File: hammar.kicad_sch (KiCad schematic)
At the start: 116 parts, among them J1 8x screw terminal, 5,08mm spa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, J10 1x2, J11 1x4, J12 1x3, J13 1x8, J14 1x3, J15 1x3, J16 1x3, J2 Micro_SD_Holder, J3 USB_C_Receptacle_USB2.0, J4 1x4, J5 1x4, J6 1x4, J7 1x4, J8 1x4, J9 1x2, Q1 S9014 or equivalent, Q2 S9014 or equivalent, Q3 TI CSD17310Q5A or equivalent, Q4 PMV40UN2R or equivalent, Q5 PMV40UN2R or equivalent, SW1 SW_MEC_5G, U1 A4988, U2 A4988, U3 A4988, U4 A4988, U5 DPAK 3,3v linear regulator + 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, U6 ESP32-WROOM-32E, U7 CH340G, Y1 Resonator_12mhz

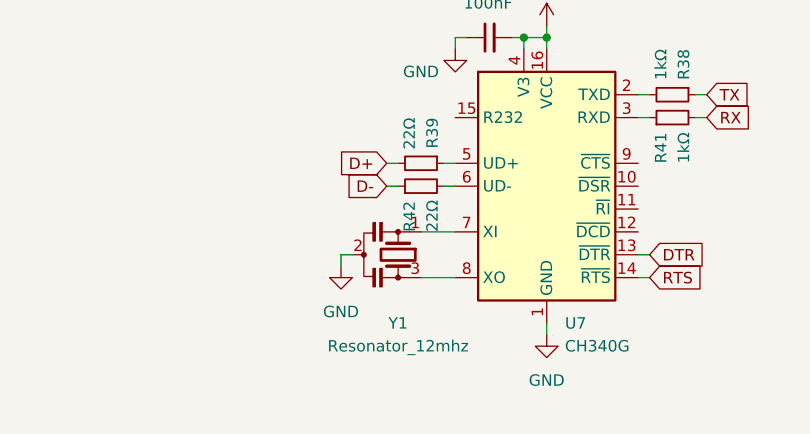
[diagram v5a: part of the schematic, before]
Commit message: replaced oscillator with crystal
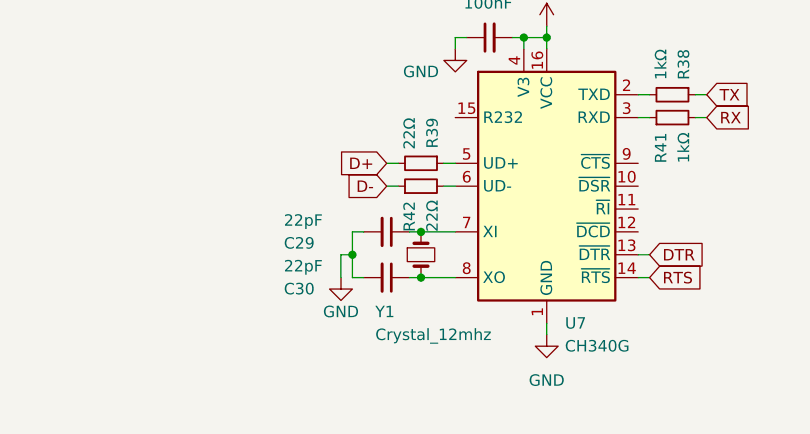
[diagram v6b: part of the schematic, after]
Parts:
- removed Y1: Resonator_12mhz, DIY:resonator_3,2x1,3, symbol Device:Resonator_Small
- added C29, C30: 22pF, Capacitor_SMD:C_0603_1608Metric, symbol Device:C_Small
- added Y1: Crystal_12mhz, Crystal:Crystal_SMD_ECS_CSM3X-2Pin_7.6x4.1mm, symbol Device:Crystal_Small
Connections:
- net GND: now also C29.2, C30.2
- net at U7.7 (XI): now also C29.1, Y1.1
- net at U7.8 (XO): now also C30.1, Y1.2
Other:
- title: Micrombo32 -> Hammar32
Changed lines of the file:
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@@
   (paper "A3")
   (title_block
-    (title "Micrombo32")
+    (title "Hammar32")
   )
   (junction (at 325.12 33.02) (diameter 0) (color 0 0 0 0)
@@
   (junction (at 382.27 21.59) (diameter 0) (color 0 0 0 0)
   )
+  (junction (at 76.2 266.7) (diameter 0) (color 0 0 0 0)
+  )
   (junction (at 138.43 55.88) (diameter 0) (color 0 0 0 0)
   )
@@
   (junction (at 95.25 242.57) (diameter 0) (color 0 0 0 0)
   )
+  (junction (at 83.82 264.16) (diameter 0) (color 0 0 0 0)
+  )
   (junction (at 339.09 143.51) (diameter 0) (color 0 0 0 0)
   )
@@
   (junction (at 185.42 33.02) (diameter 0) (color 0 0 0 0)
   )
+  (junction (at 83.82 269.24) (diameter 0) (color 0 0 0 0)
+  )
   (junction (at 294.64 77.47) (diameter 0) (color 0 0 0 0)
   )
@@
     (stroke (width 0) (type default) (color 0 0 0 0))
   )
+  (wire (pts (xy 82.55 264.16) (xy 83.82 264.16))
+    (stroke (width 0) (type default) (color 0 0 0 0))
+  )
   (wire (pts (xy 95.25 243.84) (xy 95.25 242.57))
     (stroke (width 0) (type default) (color 0 0 0 0))
@@
     (stroke (width 0) (type default) (color 0 0 0 0))
   )
-  (wire (pts (xy 74.93 267.97) (xy 74.93 266.7))
+  (wire (pts (xy 74.93 269.24) (xy 74.93 266.7))
     (stroke (width 0) (type default) (color 0 0 0 0))
   )
@@
     (stroke (width 0) (type default) (color 0 0 0 0))
   )
+  (wire (pts (xy 76.2 269.24) (xy 76.2 266.7))
+    (stroke (width 0) (type default) (color 0 0 0 0))
+  )
   (wire (pts (xy 53.34 58.42) (xy 53.34 55.88))
     (stroke (width 0) (type default) (color 0 0 0 0))
@@
     (stroke (width 0) (type default) (color 0 0 0 0))
   )
+  (wire (pts (xy 82.55 269.24) (xy 83.82 269.24))
+    (stroke (width 0) (type default) (color 0 0 0 0))
+  )
   (wire (pts (xy 91.44 82.55) (xy 91.44 83.82))
     (stroke (width 0) (type default) (color 0 0 0 0))
@@
     (stroke (width 0) (type default) (color 0 0 0 0))
   )
+  (wire (pts (xy 77.47 269.24) (xy 76.2 269.24))
+    (stroke (width 0) (type default) (color 0 0 0 0))
+  )
   (wire (pts (xy 224.79 121.92) (xy 223.52 121.92))
     (stroke (width 0) (type default) (color 0 0 0 0))
@@
     (stroke (width 0) (type default) (color 0 0 0 0))
   )
+  (wire (pts (xy 76.2 264.16) (xy 76.2 266.7))
+    (stroke (width 0) (type default) (color 0 0 0 0))
+  )
   (wire (pts (xy 387.35 227.33) (xy 387.35 224.79))
     (stroke (width 0) (type default) (color 0 0 0 0))
@@
     (stroke (width 0) (type default) (color 0 0 0 0))
   )
+  (wire (pts (xy 77.47 264.16) (xy 76.2 264.16))
+    (stroke (width 0) (type default) (color 0 0 0 0))
+  )
   (wire (pts (xy 325.12 130.81) (xy 325.12 128.27))
     (stroke (width 0) (type default) (color 0 0 0 0))
@@
     (pin "1")
   )
-  (symbol (lib_id "Device:Resonator_Small") (at 81.28 266.7 270) (unit 1)
-    (in_bom yes) (on_board yes)
-    (property "Reference" "Y1" (id 0) (at 81.28 274.32 90))
-    (property "Value" "Resonator_12mhz" (id 1) (at 81.28 276.86 90))
-    (property "Footprint" "DIY:resonator_3,2x1,3" (id 2) (at 81.28 266.065 0)
-      (effects (font (size 1.27 1.27)) hide)
-    )
-    (property "Datasheet" "~" (id 3) (at 81.28 266.065 0)
-      (effects (font (size 1.27 1.27)) hide)
-    )
-    (pin "1")
-    (pin "2")
-    (pin "3")
-  )
   (symbol (lib_id "Device:R_Small") (at 340.36 134.62 0) (unit 1)
     (in_bom yes) (on_board yes)
@@
     (pin "1")
   )
+  (symbol (lib_id "Device:C_Small") (at 80.01 269.24 270) (unit 1)
+    (in_bom yes) (on_board yes)
+    (property "Reference" "C30" (id 0) (at 68.58 270.51 90)
+      (effects (font (size 1.27 1.27)) (justify left))
+    )
+    (property "Value" "22pF" (id 1) (at 68.58 267.97 90)
+      (effects (font (size 1.27 1.27)) (justify left))
+    )
+    (property "Footprint" "Capacitor_SMD:C_0603_1608Metric" (id 2) (at 80.01 269.24 0)
+      (effects (font (size 1.27 1.27)) hide)
+    )
+    (property "Datasheet" "~" (id 3) (at 80.01 269.24 0)
+      (effects (font (size 1.27 1.27)) hide)
+    )
+    (pin "1")
+    (pin "2")
+  )
   (symbol (lib_id "Connector:Micro_SD_Card") (at 40.64 189.23 90) (unit 1)
     (in_bom yes) (on_board yes) (fields_autoplaced)
@@
     (pin "2")
   )
+  (symbol (lib_id "Device:Crystal_Small") (at 83.82 266.7 270) (unit 1)
+    (in_bom yes) (on_board yes)
+    (property "Reference" "Y1" (id 0) (at 78.74 273.05 90)
+      (effects (font (size 1.27 1.27)) (justify left))
+    )
+    (property "Value" "Crystal_12mhz" (id 1) (at 78.74 275.59 90)
+      (effects (font (size 1.27 1.27)) (justify left))
+    )
+    (property "Footprint" "Crystal:Crystal_SMD_ECS_CSM3X-2Pin_7.6x4.1mm" (id 2) (at 83.82 266.7 0)
+      (effects (font (size 1.27 1.27)) hide)
+    )
+    (property "Datasheet" "~" (id 3) (at 83.82 266.7 0)
+      (effects (font (size 1.27 1.27)) hide)
+    )
+    (pin "1")
+    (pin "2")
+  )
   (symbol (lib_id "power:GND") (at 147.32 82.55 0) (unit 1)
     (in_bom yes) (on_board yes) (fields_autoplaced)
@@
     (pin "3")
   )
+  (symbol (lib_id "Device:C_Small") (at 80.01 264.16 270) (unit 1)
+    (in_bom yes) (on_board yes)
+    (property "Reference" "C29" (id 0) (at 68.58 265.43 90)
+      (effects (font (size 1.27 1.27)) (justify left))
+    )
+    (property "Value" "22pF" (id 1) (at 68.58 262.89 90)
+      (effects (font (size 1.27 1.27)) (justify left))
+    )
+    (property "Footprint" "Capacitor_SMD:C_0603_1608Metric" (id 2) (at 80.01 264.16 0)
+      (effects (font (size 1.27 1.27)) hide)
+    )
+    (property "Datasheet" "~" (id 3) (at 80.01 264.16 0)
+      (effects (font (size 1.27 1.27)) hide)
+    )
+    (pin "1")
+    (pin "2")
+  )
   (symbol (lib_id "Device:R_Small") (at 39.37 27.94 0) (unit 1)
     (in_bom yes) (on_board yes)
@@
     (pin "1")
   )
-  (symbol (lib_id "power:GND") (at 74.93 267.97 0) (unit 1)
-    (in_bom yes) (on_board yes) (fields_autoplaced)
-    (property "Reference" "#PWR0133" (id 0) (at 74.93 274.32 0)
+  (symbol (lib_id "power:GND") (at 74.93 269.24 0) (unit 1)
+    (in_bom yes) (on_board yes)
+    (property "Reference" "#PWR0133" (id 0) (at 74.93 275.59 0)
       (effects (font (size 1.27 1.27)) hide)
     )
     (property "Value" "GND" (id 1) (at 74.93 273.05 0))
-    (property "Footprint" "" (id 2) (at 74.93 267.97 0)
+    (property "Footprint" "" (id 2) (at 74.93 269.24 0)
       (effects (font (size 1.27 1.27)) hide)
     )
-    (property "Datasheet" "" (id 3) (at 74.93 267.97 0)
+    (property "Datasheet" "" (id 3) (at 74.93 269.24 0)
       (effects (font (size 1.27 1.27)) hide)
     )
@@
       (reference "C28") (unit 1) (value "100nF") (footprint "Capacitor_SMD:C_0603_1608Metric")
     )
+    (path "/7b772451-fac7-4d9c-94c8-950628812a8c"
+      (reference "C29") (unit 1) (value "22pF") (footprint "Capacitor_SMD:C_0603_1608Metric")
+    )
+    (path "/6996feb4-43db-4675-80f0-f8913e03a32f"
+      (reference "C30") (unit 1) (value "22pF") (footprint "Capacitor_SMD:C_0603_1608Metric")
+    )
     (path "/cdb0e81e-0190-4ed4-b4e9-65c51d941267"
       (reference "D1") (unit 1) (value "LED_Small") (footprint "DIY:LED 0603 reverse mount")
@@
       (reference "U7") (unit 1) (value "CH340G") (footprint "Package_SO:SOIC-16_3.9x9.9mm_P1.27mm")
     )
-    (path "/55642e21-2468-46c2-82c3-29136dfbb9df"
-      (reference "Y1") (unit 1) (value "Resonator_12mhz") (footprint "DIY:resonator_3,2x1,3")
+    (path "/78cb5c40-df92-45aa-bf5d-b8679794bb3f"
+      (reference "Y1") (unit 1) (value "Crystal_12mhz") (footprint "Crystal:Crystal_SMD_ECS_CSM3X-2Pin_7.6x4.1mm")
     )
   )

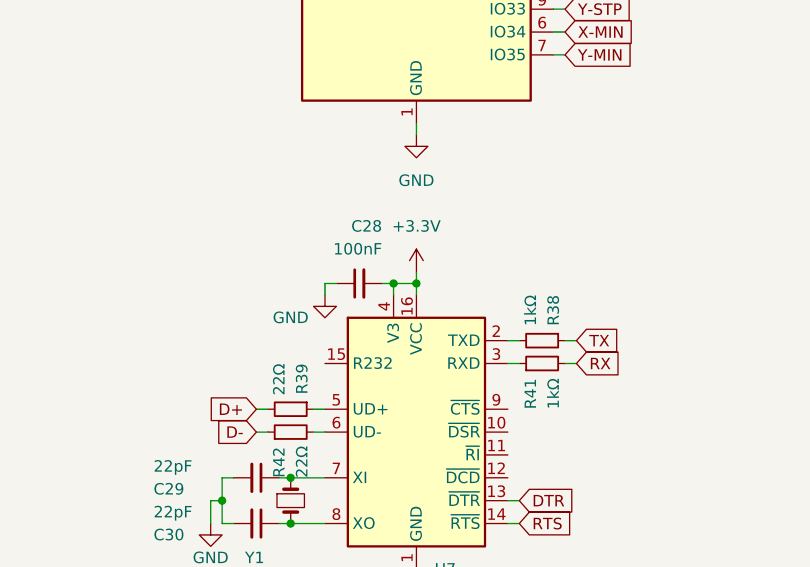
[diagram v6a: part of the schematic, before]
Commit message: removed possibly problematic trace
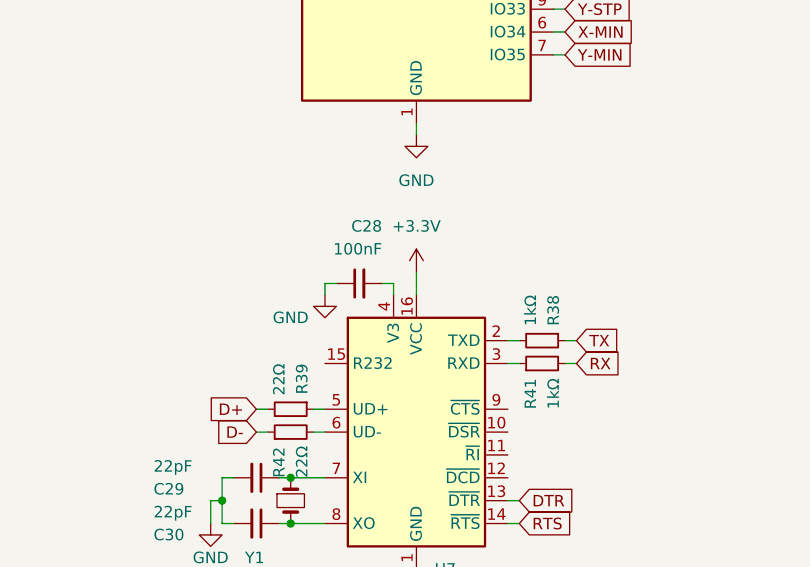
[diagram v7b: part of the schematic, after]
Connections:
- net +3.3V: no longer C28.2, U7.4 (V3)
- new net: C28.2, U7.4 (V3)
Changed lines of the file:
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@@
   (junction (at 323.85 173.99) (diameter 0) (color 0 0 0 0)
   )
-  (junction (at 95.25 242.57) (diameter 0) (color 0 0 0 0)
-  )
   (junction (at 83.82 264.16) (diameter 0) (color 0 0 0 0)
   )
@@
   )
   (junction (at 287.02 21.59) (diameter 0) (color 0 0 0 0)
-  )
-  (junction (at 97.79 242.57) (diameter 0) (color 0 0 0 0)
   )
   (junction (at 220.98 205.74) (diameter 0) (color 0 0 0 0)
@@
     (stroke (width 0) (type default) (color 0 0 0 0))
   )
-  (wire (pts (xy 97.79 241.3) (xy 97.79 242.57))
-    (stroke (width 0) (type default) (color 0 0 0 0))
-  )
   (wire (pts (xy 370.84 224.79) (xy 370.84 234.95))
     (stroke (width 0) (type default) (color 0 0 0 0))
@@
     (stroke (width 0) (type default) (color 0 0 0 0))
   )
-  (wire (pts (xy 95.25 242.57) (xy 97.79 242.57))
-    (stroke (width 0) (type default) (color 0 0 0 0))
-  )
   (wire (pts (xy 281.94 81.28) (xy 281.94 82.55))
     (stroke (width 0) (type default) (color 0 0 0 0))
@@
     (stroke (width 0) (type default) (color 0 0 0 0))
   )
-  (wire (pts (xy 97.79 242.57) (xy 97.79 243.84))
-    (stroke (width 0) (type default) (color 0 0 0 0))
-  )
+  (wire (pts (xy 97.79 241.3) (xy 97.79 243.84))
+    (stroke (width 0) (type default) (color 0 0 0 0))
+  )
